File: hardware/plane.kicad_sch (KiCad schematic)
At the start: 43 parts, among them J1 USB_B_Micro, J2 Conn_Coaxial, J3 Conn_01x03, J4 Conn_01x03, J5 Conn_01x03, J6 Conn_01x03, Q1 BSS138, Q2 BSS138, U1 ESP32-WROOM-32, U2 AMS1117-3.3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

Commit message: pcb battery connector
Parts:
- removed U8: XT30UPB-M, XT30UPB-M:XT30UPB-M, symbol XT30:XT30UPB-M
- added J7: Conn_01x02, Connector_AMASS:AMASS_XT30U-F_1x02_P5.0mm_Vertical, symbol Connector_Generic:Conn_01x02
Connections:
- net +BATT: now also J7.2 (Pin_2)
- net GND: now also J7.1 (Pin_1)
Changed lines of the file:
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@@
-	)
-	(symbol
-		(lib_id "XT30:XT30UPB-M")
-		(at 114.3 175.26 180)
-		(unit 1)
-		(exclude_from_sim no)
-		(in_bom yes)
-		(on_board yes)
-		(dnp no)
-		(fields_autoplaced yes)
-		(property "Reference" "U8"
-			(at 118.11 175.2599 0)
-			(effects
-				(font
-					(size 1.27 1.27)
-				)
-				(justify right)
-			)
-		)
-		(property "Value" "XT30UPB-M"
-			(at 118.11 177.7999 0)
-			(effects
-				(font
-					(size 1.27 1.27)
-				)
-				(justify right)
-			)
-		)
-		(property "Footprint" "XT30UPB-M:XT30UPB-M"
-			(at 114.3 175.26 0)
-			(effects
-				(font
-					(size 1.27 1.27)
-				)
-				(justify bottom)
-				(hide yes)
-			)
-		)
-		(property "Datasheet" ""
-			(at 114.3 175.26 0)
-			(effects
-				(font
-					(size 1.27 1.27)
-				)
-				(hide yes)
-			)
-		)
-		(property "Description" ""
-			(at 114.3 175.26 0)
-			(effects
-				(font
-					(size 1.27 1.27)
-				)
-				(hide yes)
-			)
-		)
-		(property "MF" "amass"
-			(at 114.3 175.26 0)
-			(effects
-				(font
-					(size 1.27 1.27)
-				)
-				(justify bottom)
-				(hide yes)
-			)
-		)
-		(property "Description_1" "\nSocket; DC supply; XT30; male; PIN: 2; on PCBs; THT; yellow; 15A; 500V\n"
-			(at 114.3 175.26 0)
-			(effects
-				(font
-					(size 1.27 1.27)
-				)
-				(justify bottom)
-				(hide yes)
-			)
-		)
-		(property "Package" "None"
-			(at 114.3 175.26 0)
-			(effects
-				(font
-					(size 1.27 1.27)
-				)
-				(justify bottom)
-				(hide yes)
-			)
-		)
-		(property "Price" "None"
-			(at 114.3 175.26 0)
-			(effects
-				(font
-					(size 1.27 1.27)
-				)
-				(justify bottom)
-				(hide yes)
-			)
-		)
-		(property "SnapEDA_Link" "https://www.snapeda.com/parts/XT30UPB-M/AMASS/view-part/?ref=snap"
-			(at 114.3 175.26 0)
-			(effects
-				(font
-					(size 1.27 1.27)
-				)
-				(justify bottom)
-				(hide yes)
-			)
-		)
-		(property "MP" "XT30UPB-M"
-			(at 114.3 175.26 0)
-			(effects
-				(font
-					(size 1.27 1.27)
-				)
-				(justify bottom)
-				(hide yes)
-			)
-		)
-		(property "Availability" "Not in stock"
-			(at 114.3 175.26 0)
-			(effects
-				(font
-					(size 1.27 1.27)
-				)
-				(justify bottom)
-				(hide yes)
-			)
-		)
-		(property "Check_prices" "https://www.snapeda.com/parts/XT30UPB-M/AMASS/view-part/?ref=eda"
-			(at 114.3 175.26 0)
-			(effects
-				(font
-					(size 1.27 1.27)
-				)
-				(justify bottom)
-				(hide yes)
-			)
-		)
-		(pin "P$2"
-		)
-		(pin "P$1"
-		)
-		(instances
-			(project ""
-				(path "/da86c4d3-eb89-47ad-a94a-ba8dff9acc70"
-					(reference "U8")
-					(unit 1)
-				)
-			)
-		)
 	)
 	(symbol
@@
 					(unit 1)
 				)
+			)
+		)
+	)
+	(symbol
+		(lib_id "Connector_Generic:Conn_01x02")
+		(at 111.76 175.26 0)
+		(unit 1)
+		(exclude_from_sim no)
+		(in_bom yes)
+		(on_board yes)
+		(dnp no)
+		(fields_autoplaced yes)
+		(property "Reference" "J7"
+			(at 114.3 175.2599 0)
+			(effects
+				(font
+					(size 1.27 1.27)
+				)
+				(justify left)
+			)
+		)
+		(property "Value" "Conn_01x02"
+			(at 114.3 177.7999 0)
+			(effects
+				(font
+					(size 1.27 1.27)
+				)
+				(justify left)
+			)
+		)
+		(property "Footprint" "Connector_AMASS:AMASS_XT30U-F_1x02_P5.0mm_Vertical"
+			(at 111.76 175.26 0)
+			(effects
+				(font
+					(size 1.27 1.27)
+				)
+				(hide yes)
+			)
+		)
+		(property "Datasheet" "~"
+			(at 111.76 175.26 0)
+			(effects
+				(font
+					(size 1.27 1.27)
+				)
+				(hide yes)
+			)
+		)
+		(property "Description" "Generic connector, single row, 01x02, script generated (kicad-library-utils/schlib/autogen/connector/)"
+			(at 111.76 175.26 0)
+			(effects
+				(font
+					(size 1.27 1.27)
+				)
+				(hide yes)
+			)
+		)
+		(pin "2"
+		)
+		(pin "1"
+		)
+		(instances
+			(project ""
+				(path "/da86c4d3-eb89-47ad-a94a-ba8dff9acc70"
+					(reference "J7")
+					(unit 1)
+				)

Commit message: add esc connector
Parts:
- added TP1, TP2, TP3: TestPoint, TestPoint:TestPoint_Pad_2.5x2.5mm, symbol Connector:TestPoint
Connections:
- net +BATT: now also TP2.1
- net GND: now also TP3.1
- net MOTOR: now reaches U1.9 (IO33)
- net MOTOR: now also TP1.1
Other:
- note added: "BATTERY CONNECTOR"
- note added: "ESC CONTROL"

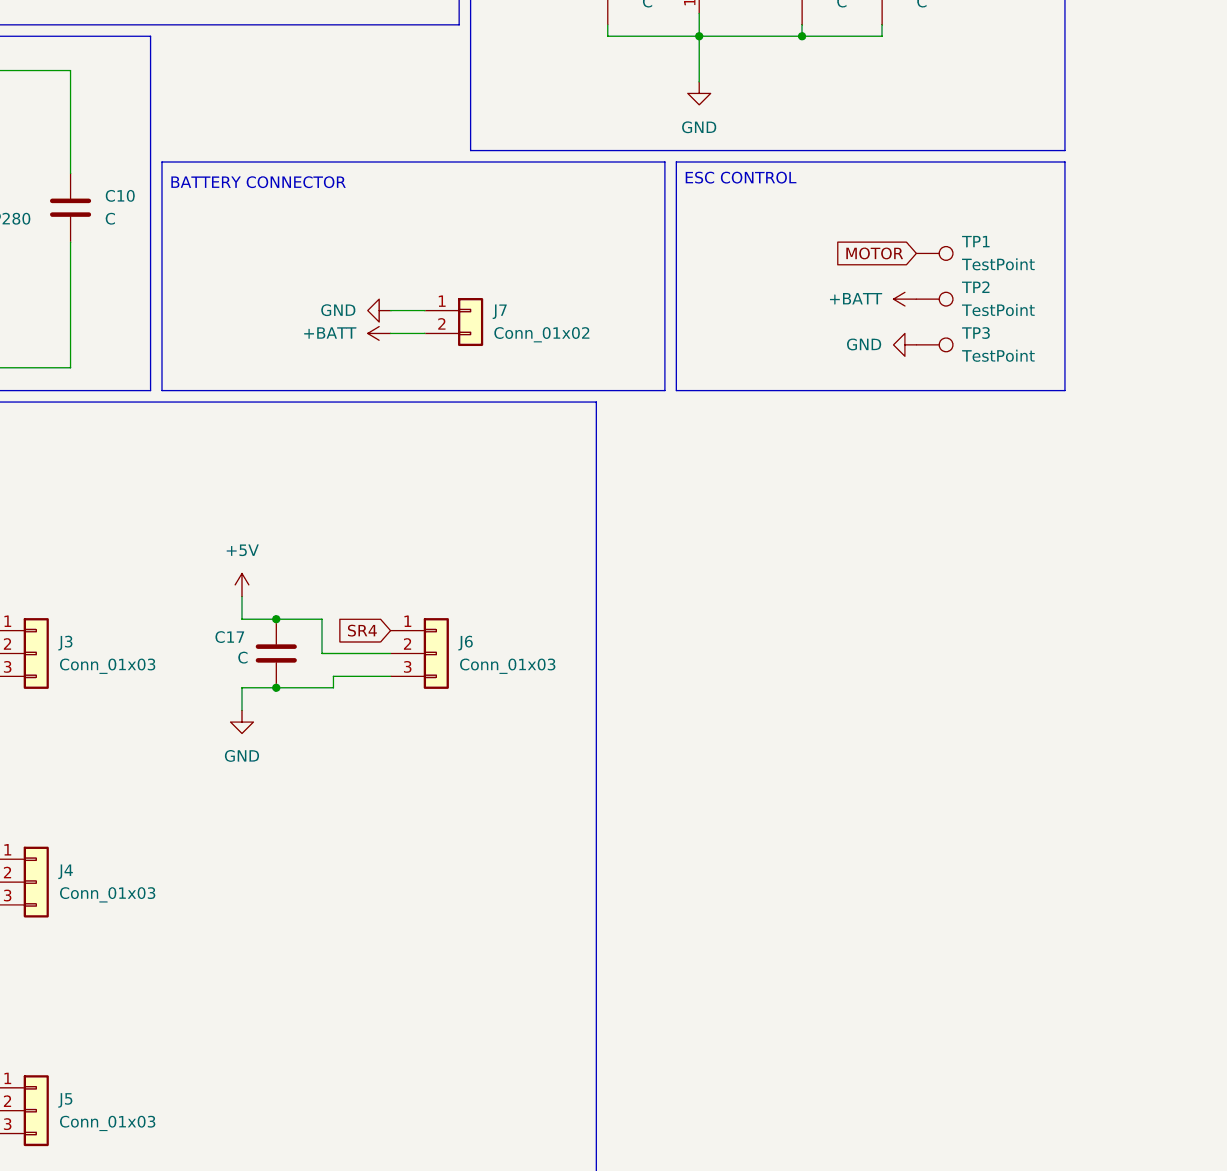
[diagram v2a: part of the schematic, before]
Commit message: upgrade esc connector & sma
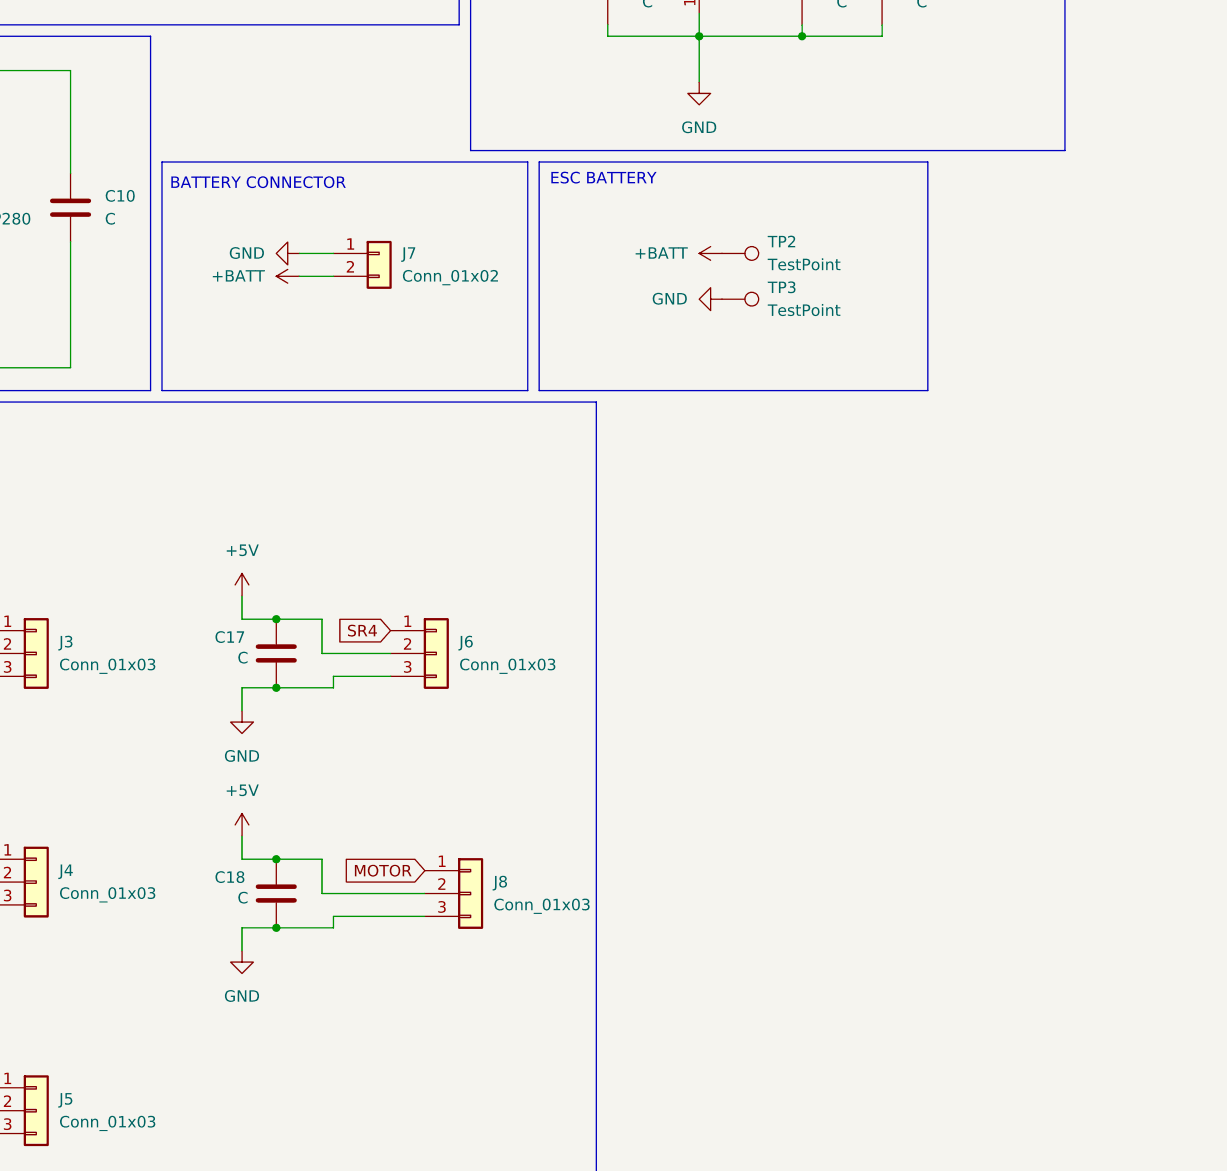
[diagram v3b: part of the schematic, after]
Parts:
- removed TP1: TestPoint, TestPoint:TestPoint_Pad_2.5x2.5mm, symbol Connector:TestPoint
- added C18: C, Capacitor_SMD:C_0603_1608Metric, symbol Device:C
- added J8: Conn_01x03, Connector_PinHeader_2.54mm:PinHeader_1x03_P2.54mm_Vertical, symbol Connector_Generic:Conn_01x03
- J2: footprint Connector_Coaxial:SMA_Amphenol_132289_EdgeMount -> Connector_Coaxial:SMA_Samtec_SMA-J-P-H-ST-EM1_EdgeMount
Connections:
- net +5V: now also C18.1, J8.2 (Pin_2)
- net GND: now also C18.2, J8.3 (Pin_3)
- net MOTOR: now also J8.1 (Pin_1)
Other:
- note added: "ESC BATTERY"
- note removed: "ESC CONTROL"
- moved on the sheet: J7, TP2, TP3

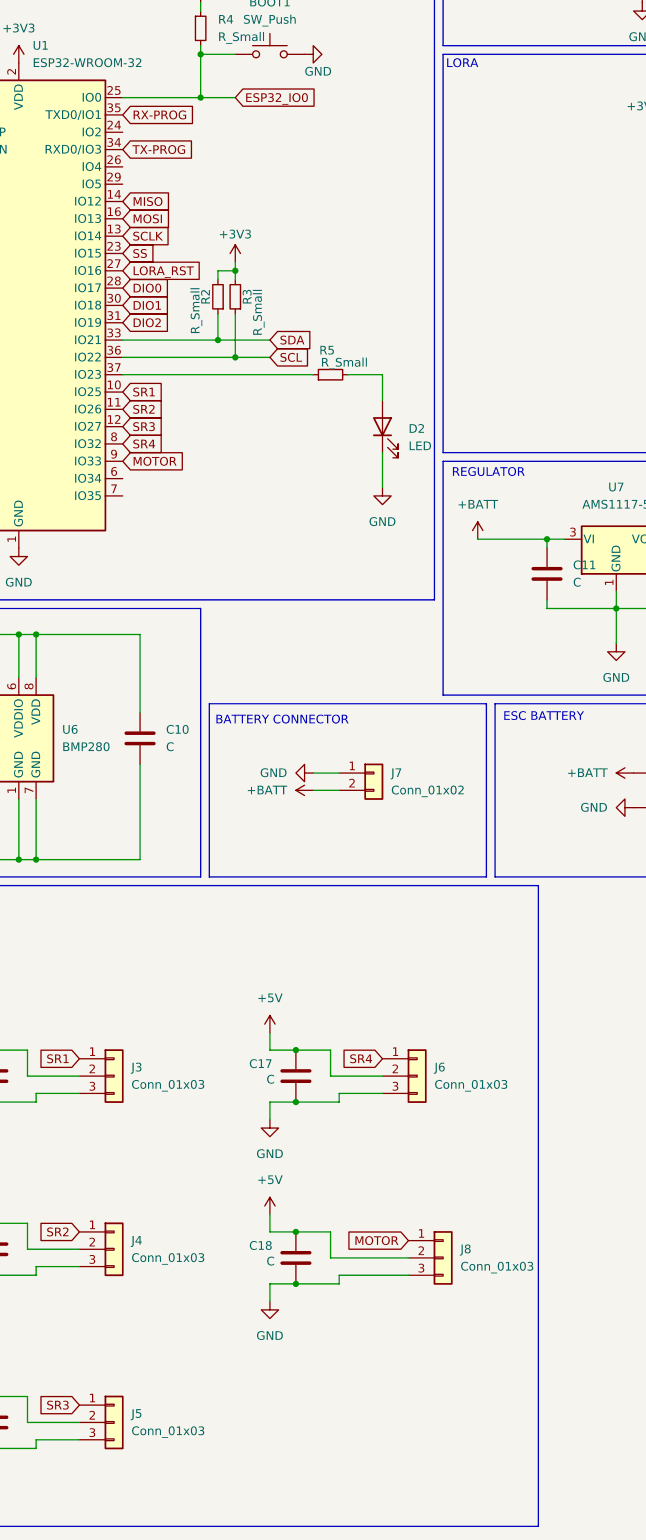
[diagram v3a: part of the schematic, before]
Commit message: add servo connector
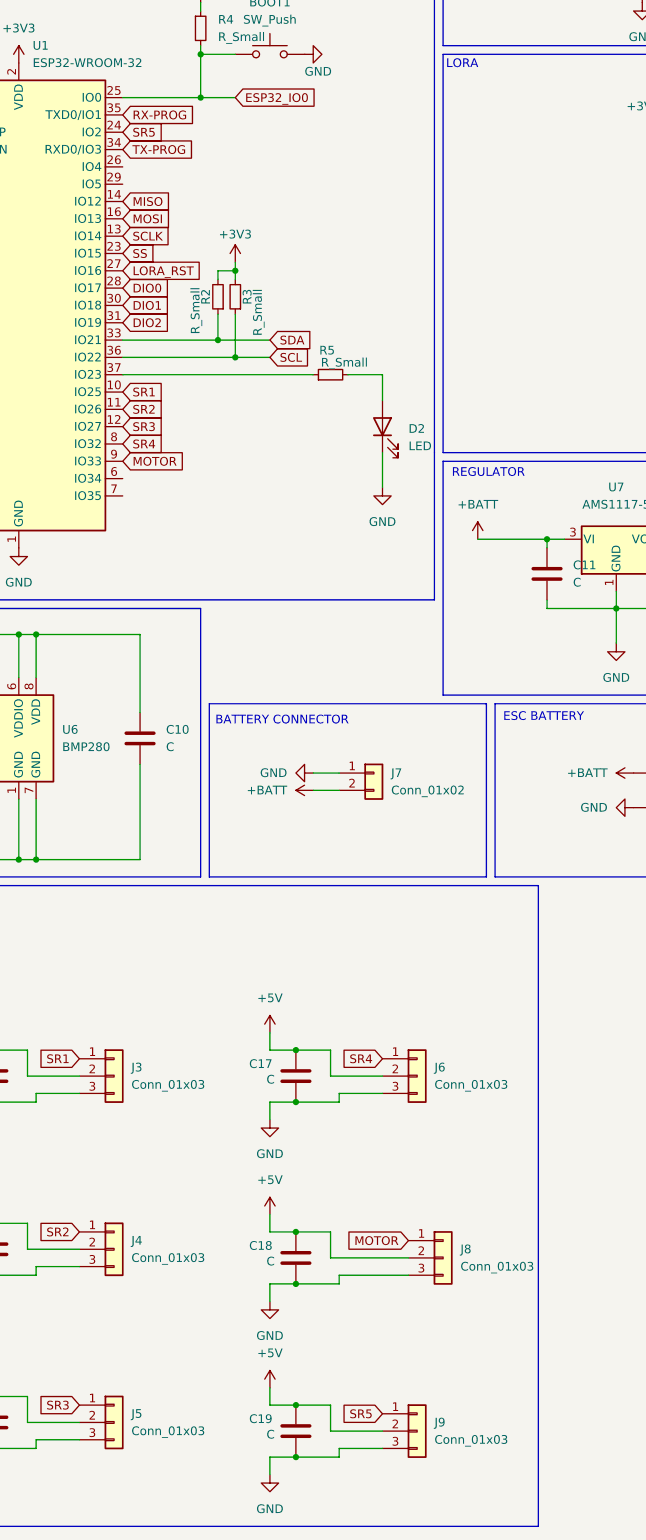
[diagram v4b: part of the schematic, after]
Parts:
- added C19: C, Capacitor_SMD:C_0603_1608Metric, symbol Device:C
- added J9: Conn_01x03, Connector_PinHeader_2.54mm:PinHeader_1x03_P2.54mm_Vertical, symbol Connector_Generic:Conn_01x03
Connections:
- net +5V: now also C19.1, J9.2 (Pin_2)
- net GND: now also C19.2, J9.3 (Pin_3)
- net SR5: now reaches U1.24 (IO2)
- net SR5: now also J9.1 (Pin_1)

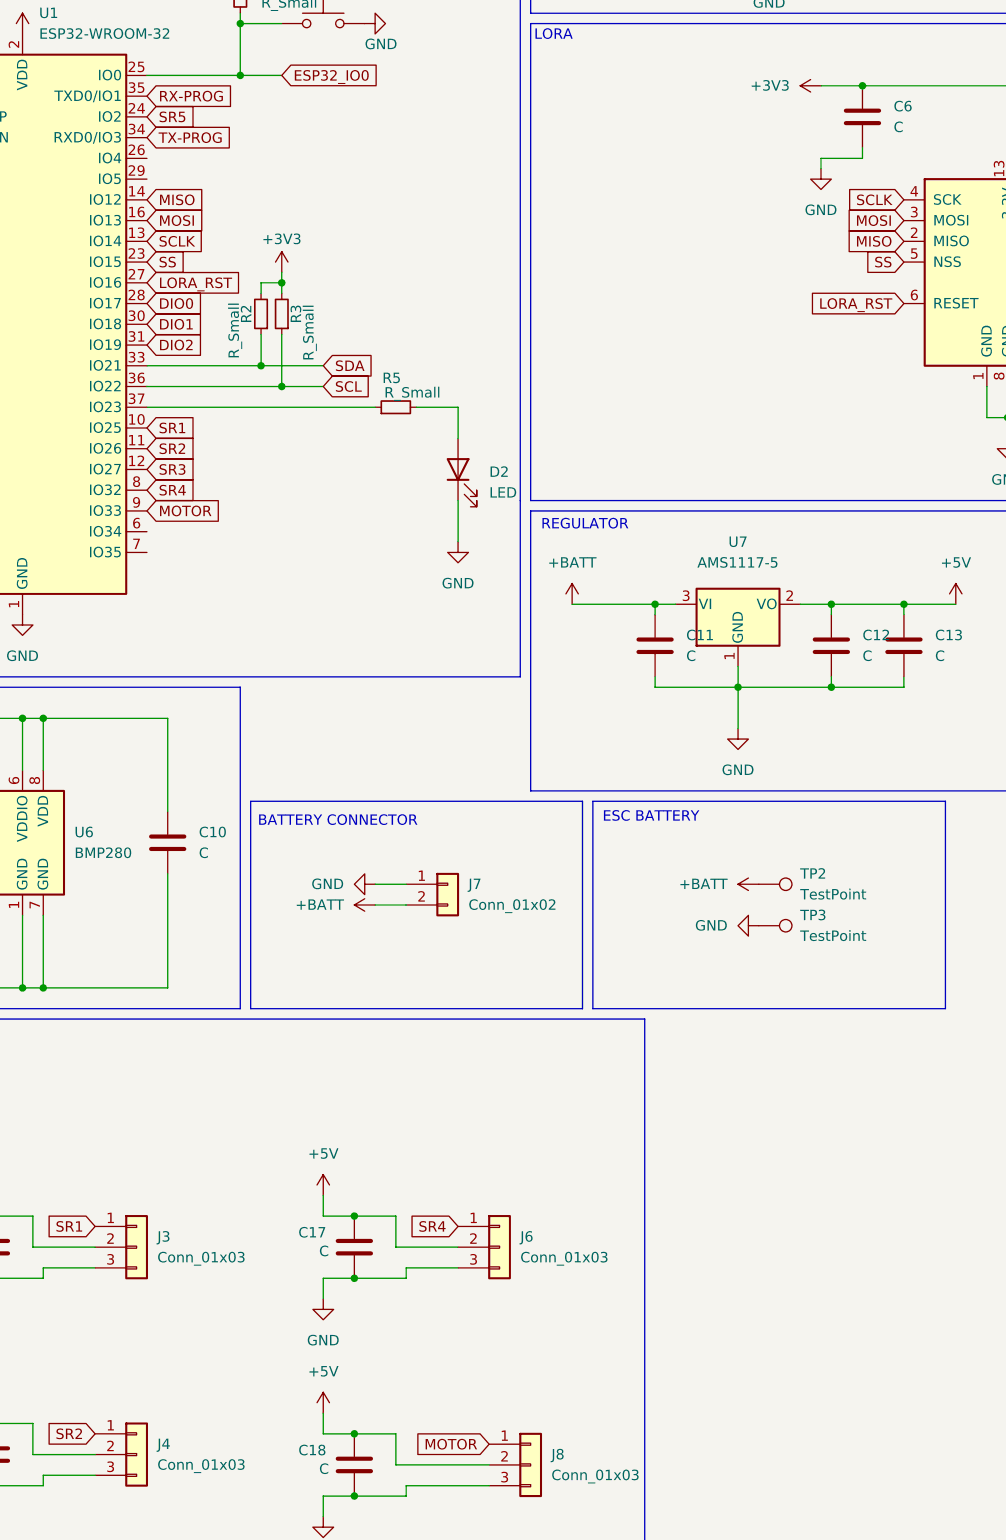
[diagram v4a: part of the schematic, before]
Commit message: add i2c and uart connectors
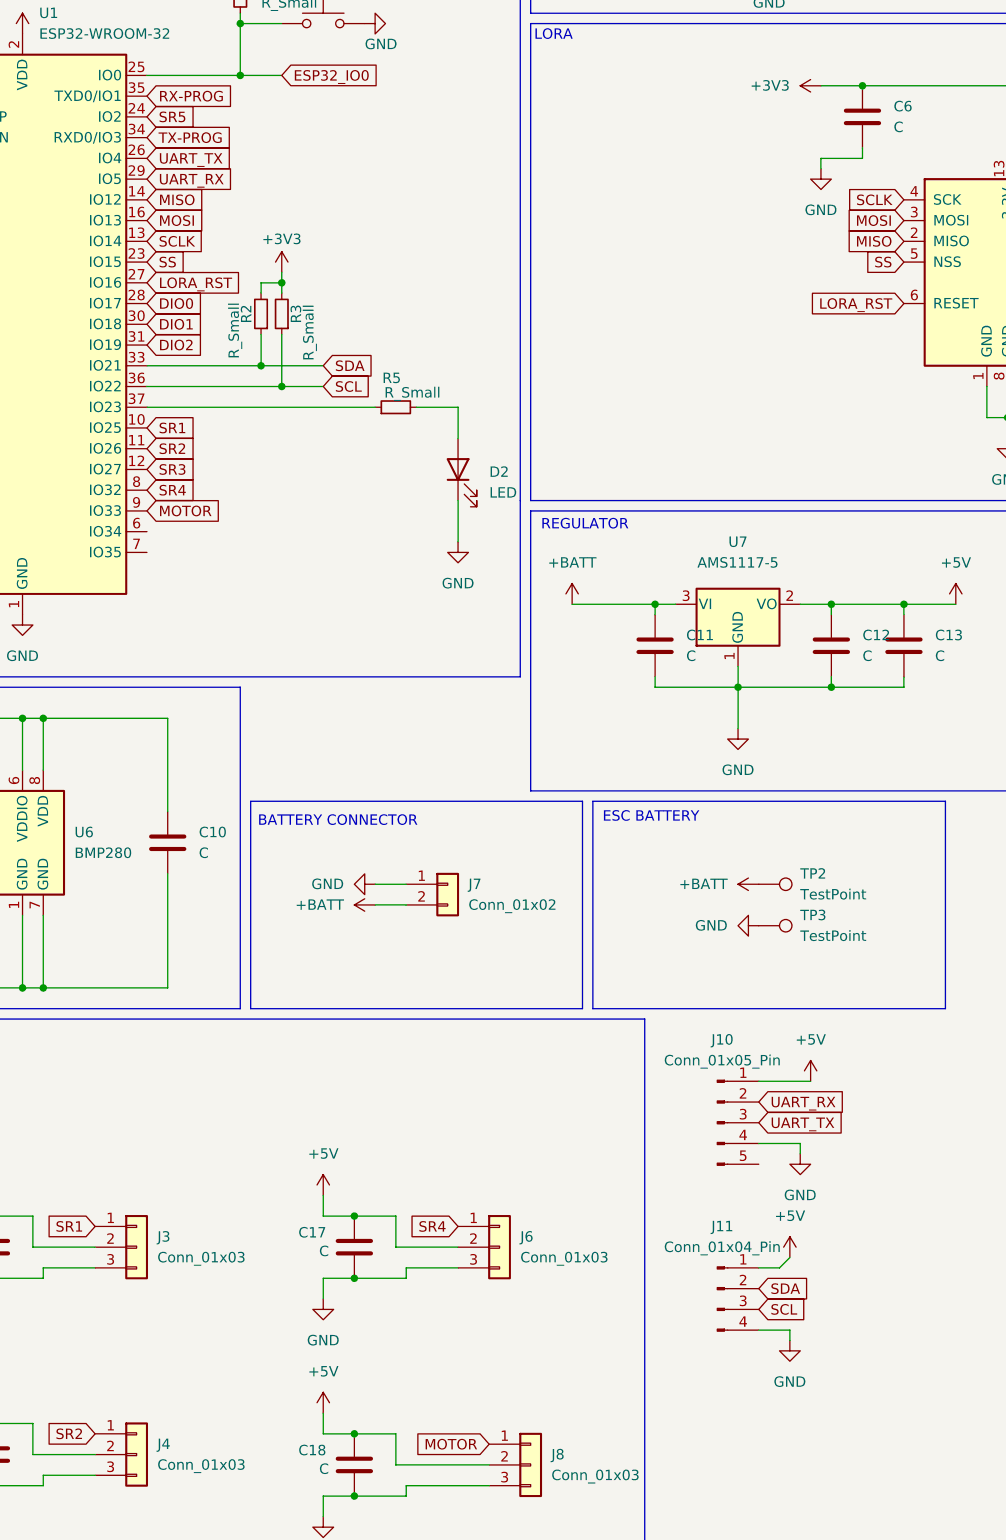
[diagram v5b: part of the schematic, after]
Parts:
- added J10: Conn_01x05_Pin, Connector_PinHeader_2.54mm:PinHeader_1x05_P2.54mm_Vertical, symbol Connector:Conn_01x05_Pin
- added J11: Conn_01x04_Pin, Connector_PinHeader_2.54mm:PinHeader_1x04_P2.54mm_Vertical, symbol Connector:Conn_01x04_Pin
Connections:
- net +5V: now also J10.1 (Pin_1), J11.1 (Pin_1)
- net GND: now also J10.4 (Pin_4), J11.4 (Pin_4)
- net SCL: now also J11.3 (Pin_3)
- net SDA: now also J11.2 (Pin_2)
- net UART_TX: now reaches U1.26 (IO4)
- net UART_TX: now also J10.3 (Pin_3)
- net UART_RX: now reaches U1.29 (IO5)
- net UART_RX: now also J10.2 (Pin_2)
